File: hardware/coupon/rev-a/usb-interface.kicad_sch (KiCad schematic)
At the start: 13 parts, among them J1 USB4505-03-0-A, U29 TPS70933DBVR, U31 TUSB320LAIRWBR, U32 TS3USB31ERSER, U33 TPD4E05U06DQAR

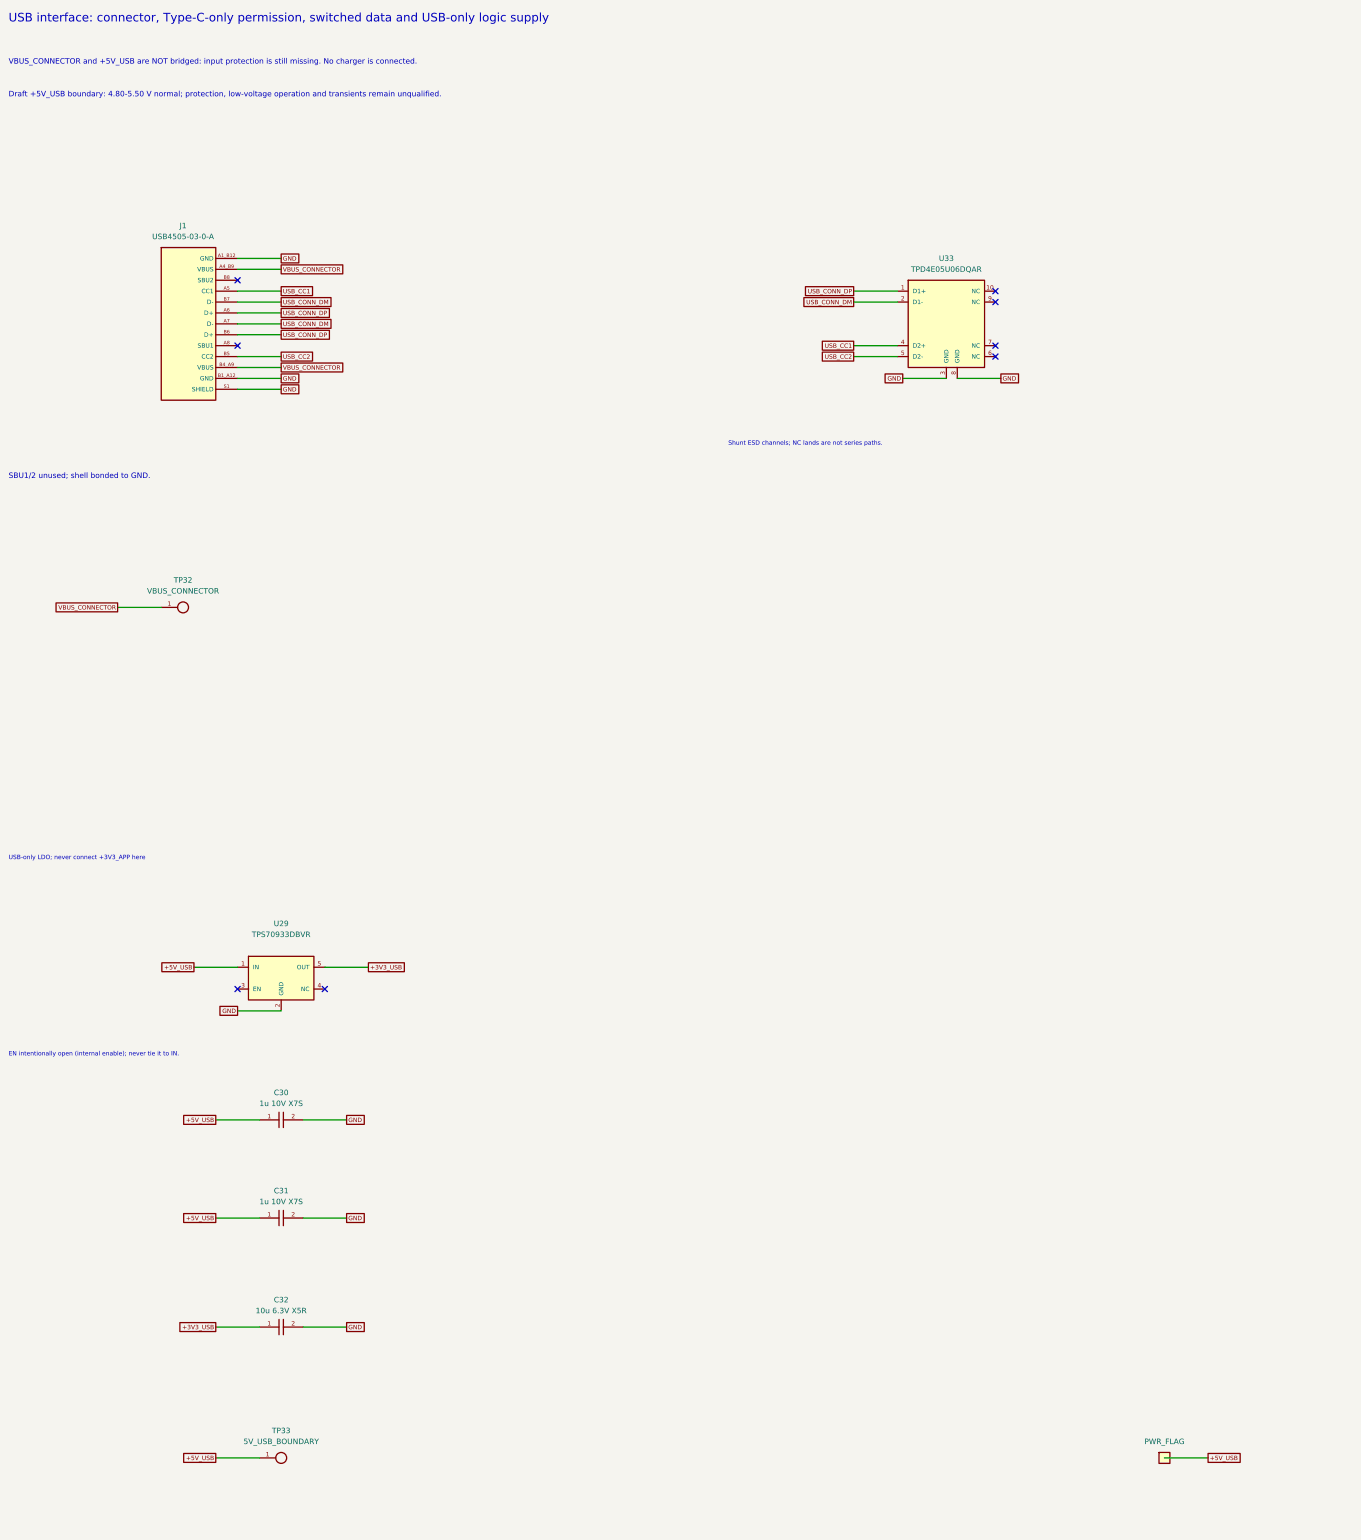
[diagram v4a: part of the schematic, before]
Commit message: Capture provisional E0 protected USB source bridge
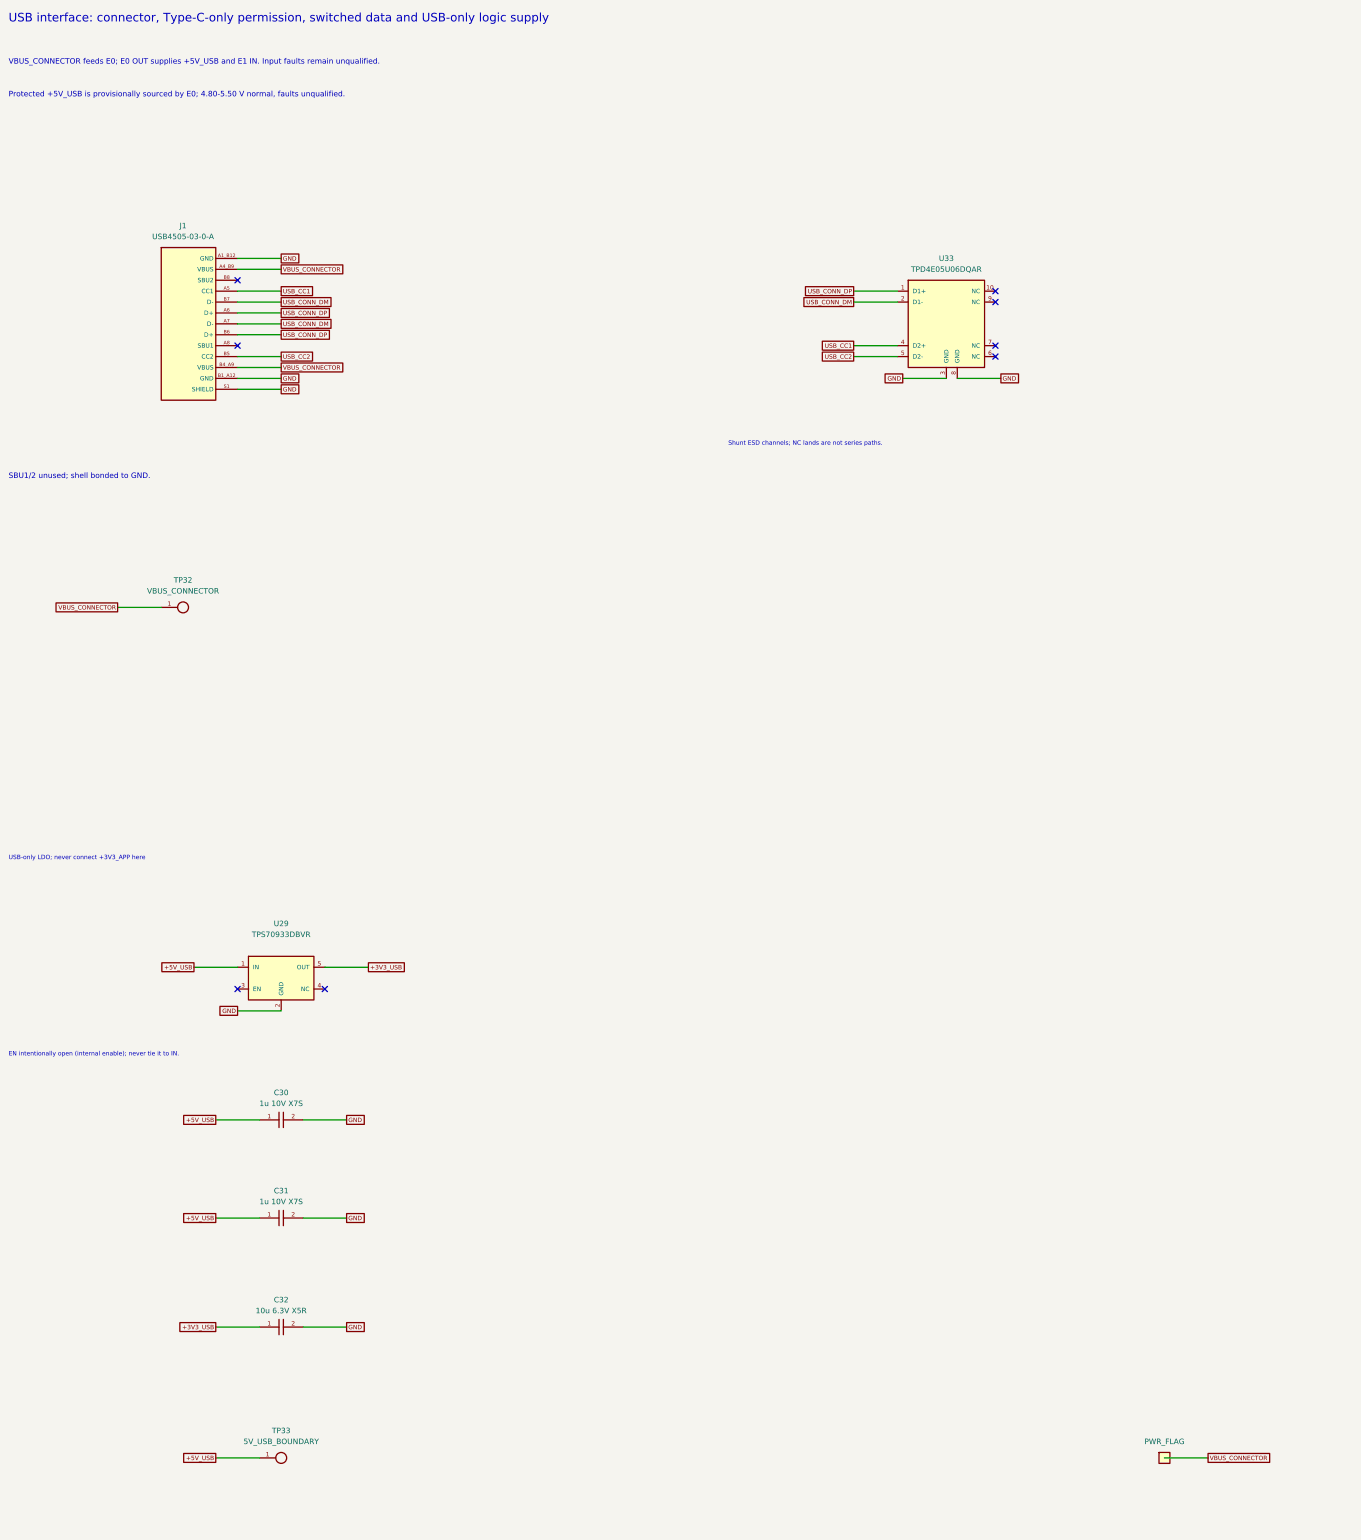
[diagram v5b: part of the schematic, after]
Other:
- note added: "Protected +5V_USB is provisionally sourced by E0; 4.80-5.50 V normal, faults unqualified."
- note added: "VBUS_CONNECTOR feeds E0; E0 OUT supplies +5V_USB and E1 IN. Input faults remain unqualified."
- note removed: "Draft +5V_USB boundary: 4.80-5.50 V normal; protection, low-voltage operation and transients remain unqualified."
- note removed: "VBUS_CONNECTOR and +5V_USB are NOT bridged: input protection is still missing. No charger is connected."
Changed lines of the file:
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@@
 (title_block (title "Coupon Rev A - USB detection, data and logic supply") (rev "A-draft") (comment 1 "SPDX-License-Identifier: CERN-OHL-S-2.0") (comment 2 "Input protection, supervisors and charger actuation remain open"))
 (text "USB interface: connector, Type-C-only permission, switched data and USB-only logic supply" (at 20.320 20.320 0) (effects (font (size 2 2)) (justify left)))
-(text "VBUS_CONNECTOR and +5V_USB are NOT bridged: input protection is still missing. No charger is connected." (at 20.320 30.480 0) (effects (font (size 1.27 1.27)) (justify left)))
-(text "Draft +5V_USB boundary: 4.80-5.50 V normal; protection, low-voltage operation and transients remain unqualified." (at 20.320 38.100 0) (effects (font (size 1.27 1.27)) (justify left)))
+(text "VBUS_CONNECTOR feeds E0; E0 OUT supplies +5V_USB and E1 IN. Input faults remain unqualified." (at 20.320 30.480 0) (effects (font (size 1.27 1.27)) (justify left)))
+(text "Protected +5V_USB is provisionally sourced by E0; 4.80-5.50 V normal, faults unqualified." (at 20.320 38.100 0) (effects (font (size 1.27 1.27)) (justify left)))
 (symbol (lib_id "rgb-badge-coupon:USB4505-03-0-A") (at 60.960 91.440 0) (unit 1)
 (exclude_from_sim no) (in_bom yes) (on_board yes) (dnp no)
@@
 (instances (project "rgb-badge-coupon" (path "/207fb68e-2ddb-46bb-8712-eba2f8c5eef6/271a5e22-dd9f-53e5-be76-9ea876726439" (reference "#FLG05") (unit 1)))))
 (wire (pts (xy 289.560 355.600) (xy 299.720 355.600)) (stroke (width 0) (type default)))
-(global_label "+5V_USB" (shape passive) (at 299.720 355.600 0) (effects (font (size 1.016 1.016)) (justify left)) (property "Intersheetrefs" "${INTERSHEET_REFS}" (at 299.720 355.600 0) (effects (font (size 1.27 1.27)) (hide yes))))
+(global_label "VBUS_CONNECTOR" (shape passive) (at 299.720 355.600 0) (effects (font (size 1.016 1.016)) (justify left)) (property "Intersheetrefs" "${INTERSHEET_REFS}" (at 299.720 355.600 0) (effects (font (size 1.27 1.27)) (hide yes))))
 (text "Effective capacitance, inrush, total-port current, undervoltage/ramp behavior and input protection remain open." (at 20.320 381.000 0) (effects (font (size 1.27 1.27)) (justify left)))
 (text "R60/R61 provide Type-C output pull-ups. USB-A/default-current sources: data only while ON, no charging." (at 20.320 391.160 0) (effects (font (size 1.016 1.016)) (justify left)))

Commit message: Correct all six exact Murata capacitor lands and preserve 59-edge routing
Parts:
- C32: footprint rgb-badge-coupon:C_Murata_GRM18_0603 -> rgb-badge-coupon:C_Murata_GRM188R60J106ME47_0603
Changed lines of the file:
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@@
 (property "Reference" "C32" (at 83.820 318.770 0) (effects (font (size 1.27 1.27))))
 (property "Value" "10u 6.3V X5R" (at 83.820 321.310 0) (effects (font (size 1.27 1.27))))
-(property "Footprint" "rgb-badge-coupon:C_Murata_GRM18_0603" (at 83.820 325.120 0) (effects (font (size 1.27 1.27)) (hide yes)))
+(property "Footprint" "rgb-badge-coupon:C_Murata_GRM188R60J106ME47_0603" (at 83.820 325.120 0) (effects (font (size 1.27 1.27)) (hide yes)))
 (property "Datasheet" "https://pim.murata.com/en-global/pim/details/?partNum=GRM188R60J106ME47D" (at 83.820 325.120 0) (effects (font (size 1.27 1.27)) (hide yes)))
 (property "Manufacturer" "Murata" (at 83.820 325.120 0) (effects (font (size 1.27 1.27)) (hide yes)))
